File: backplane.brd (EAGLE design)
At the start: 203.2 x 101.6 mm, 14 parts, among them IC1 MAX3233ECWP

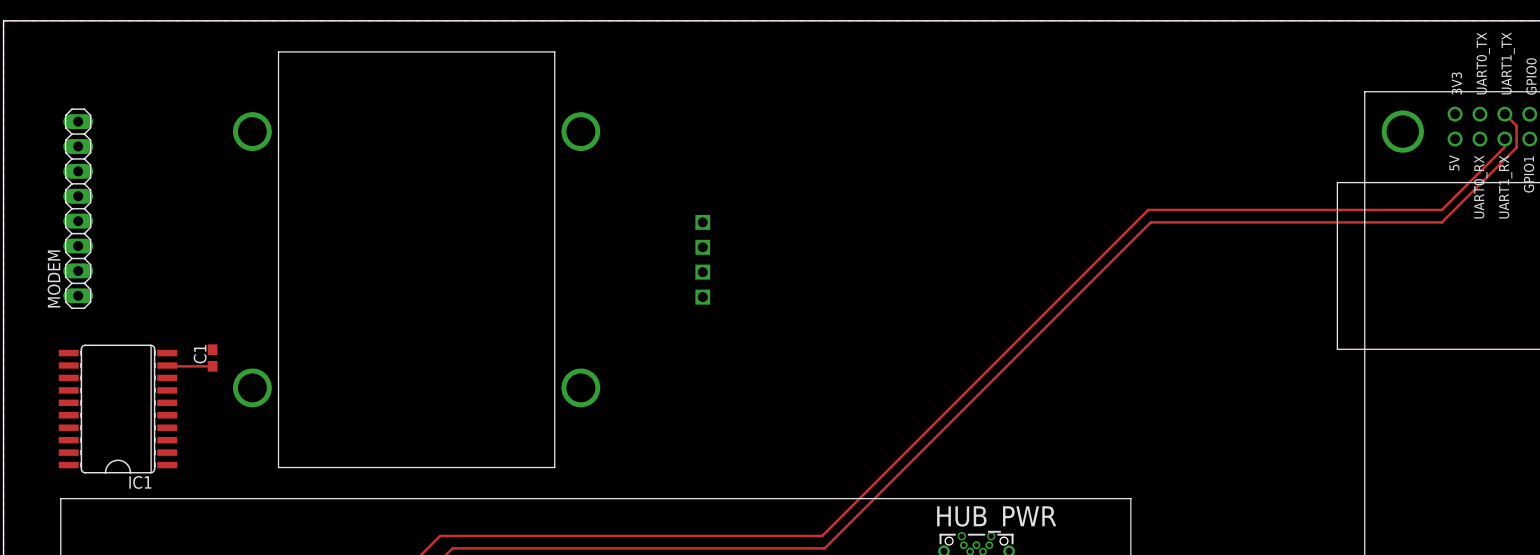
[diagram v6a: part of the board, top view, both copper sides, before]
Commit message: Add jetson - converter uart connection
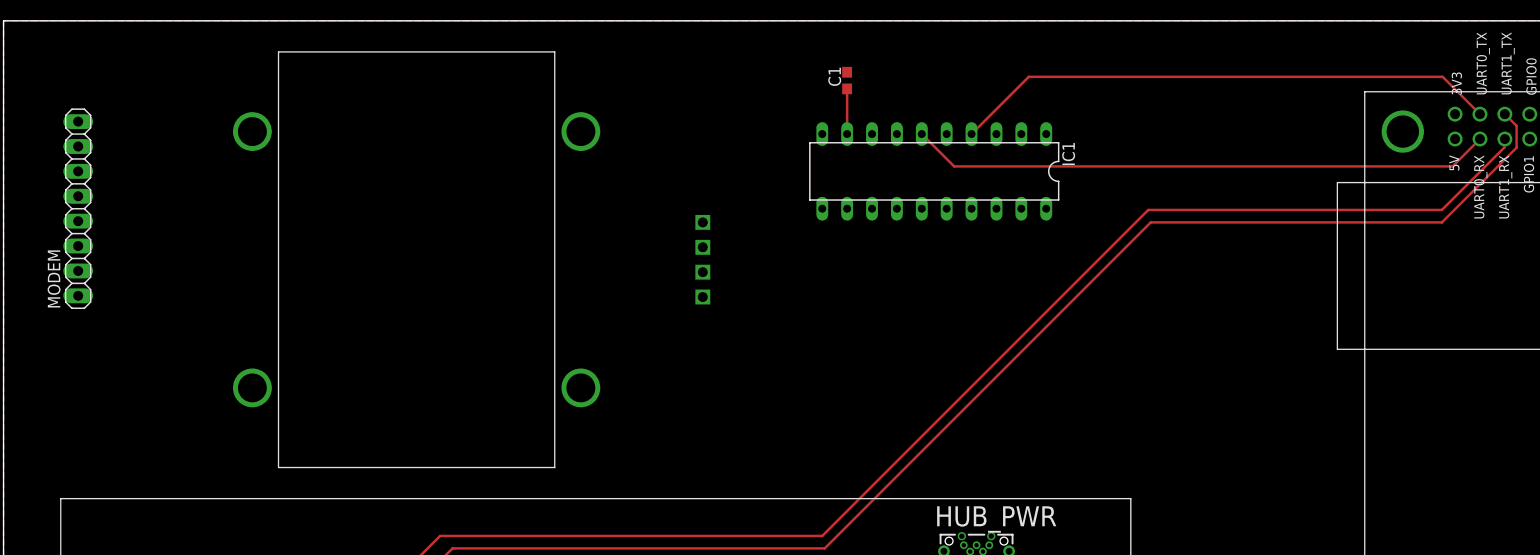
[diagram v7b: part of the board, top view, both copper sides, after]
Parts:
- C1: value (none) -> 0.1uF
- IC1: value MAX3233ECWP -> MAX3233ECPP; device auv:SO20L -> auv:DIL20
- moved IC1 86.8 mm to (95.0, 86.2), turned to 180 degrees
- moved C1 70.7 mm to (86.1, 95.5)
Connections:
- removed net SPARTON_RX: U$3.UART0_TX
- removed net SPARTON_TX: U$3.UART0_RX
- net MODEM_RS232_RX: now also IC1.7; no longer IC1.8
- net MODEM_RS232_TX: now also IC1.8; no longer IC1.7
- net MODEM_RX: now also IC1.4, U$3.UART0_TX; no longer IC1.6
- net MODEM_TX: now also IC1.6, U$3.UART0_RX; no longer IC1.4
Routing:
- net MODEM_TX: track 0.00 -> 59.5 mm
- net MODEM_RX: track 0.00 -> 55.9 mm
- added copper zone on layer 1, net GND
- added copper zone on layer 16, net VBAT
- removed copper zone on layer 16, net GND
- removed copper zone on layer 1, net VBAT
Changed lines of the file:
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@@
 <element name="PIXHAWK" library="auv" package="TE-2-5530843-0" value="PIXHAWK_EDGE_CONNCONN" x="70.612" y="30.734"/>
 <element name="MODEM" library="auv" package="1X08" value="" x="7.62" y="82.423" rot="R90"/>
-<element name="IC1" library="auv" package="SO20L" value="MAX3233ECWP" x="11.684" y="61.976" rot="R90">
-<attribute name="MF" value="MAXIM" x="11.684" y="61.976" size="1.778" layer="27" rot="R90" display="off"/>
-<attribute name="MPN" value="MAX3233ECWP" x="11.684" y="61.976" size="1.778" layer="27" rot="R90" display="off"/>
-<attribute name="OC_FARNELL" value="unknown" x="11.684" y="61.976" size="1.778" layer="27" rot="R90" display="off"/>
-<attribute name="OC_NEWARK" value="77C9167" x="11.684" y="61.976" size="1.778" layer="27" rot="R90" display="off"/>
+<element name="IC1" library="auv" package="DIL20" value="MAX3233ECPP" x="94.996" y="86.233" rot="R180">
+<attribute name="MF" value="" x="94.996" y="86.233" size="1.778" layer="27" rot="R180" display="off"/>
+<attribute name="MPN" value="MAX3233ECPP+G36" x="94.996" y="86.233" size="1.778" layer="27" rot="R180" display="off"/>
+<attribute name="OC_FARNELL" value="unknown" x="94.996" y="86.233" size="1.778" layer="27" rot="R180" display="off"/>
+<attribute name="OC_NEWARK" value="89K3596" x="94.996" y="86.233" size="1.778" layer="27" rot="R180" display="off"/>
 </element>
-<element name="C1" library="auv" package="C0603" value="" x="21.336" y="67.183" rot="R90"/>
+<element name="C1" library="auv" package="C0603" value="0.1uF" x="86.106" y="95.504" rot="R90"/>
 </elements>
 <signals>
@@
 <contactref element="HUB_PWR" pad="10"/>
 <contactref element="HUB_PWR" pad="6"/>
-<polygon width="0.1524" layer="16">
-<vertex x="203.2" y="101.6"/>
-<vertex x="0" y="101.6"/>
-<vertex x="0" y="0"/>
-<vertex x="203.2" y="0"/>
-</polygon>
 <contactref element="U$1" pad="GND"/>
 <contactref element="BAT" pad="P$2"/>
@@
 <contactref element="IC1" pad="18"/>
 <contactref element="C1" pad="2"/>
-<wire x1="6.6548" y1="58.801" x2="21.336" y2="68.033" width="0" layer="19" extent="1-1"/>
-<wire x1="8.128" y1="33.431" x2="6.6548" y2="58.801" width="0" layer="19" extent="1-1"/>
-</signal>
-<signal name="VBAT">
-<contactref element="U$3" pad="VIN"/>
 <polygon width="0.1524" layer="1">
 <vertex x="0" y="101.6"/>
@@
 <vertex x="0" y="0"/>
 </polygon>
+</signal>
+<signal name="VBAT">
+<contactref element="U$3" pad="VIN"/>
 <contactref element="BAT" pad="P$1"/>
+<polygon width="0.1524" layer="16">
+<vertex x="203.2" y="101.6"/>
+<vertex x="0" y="101.6"/>
+<vertex x="0" y="0"/>
+<vertex x="203.2" y="0"/>
+</polygon>
 </signal>
 <signal name="PIXHAWK_TELEM2_TX">
@@
 <wire x1="169.8244" y1="98.5012" x2="193.3194" y2="98.5012" width="0.254" layer="1"/>
 <wire x1="193.3194" y1="98.5012" x2="193.3194" y2="91.9988" width="0.254" layer="1"/>
-</signal>
-<signal name="SPARTON_RX">
-<contactref element="U$3" pad="UART0_TX"/>
 </signal>
 <signal name="+5V">
@@
 <wire x1="197.8406" y1="81.8388" x2="197.8406" y2="88.3412" width="0" layer="19" extent="1-1"/>
 </signal>
-<signal name="SPARTON_TX">
-<contactref element="U$3" pad="UART0_RX"/>
-</signal>
 <signal name="AHRS8_RX">
 <contactref element="U$1" pad="RX"/>
@@
 <wire x1="158.3182" y1="77.9018" x2="158.3182" y2="89.535" width="0.254" layer="16"/>
 </signal>
-<signal name="MODEM_RS232_TX">
+<signal name="MODEM_RS232_RX">
 <contactref element="IC1" pad="7"/>
 </signal>
-<signal name="MODEM_RS232_RX">
-<contactref element="IC1" pad="8"/>
-</signal>
-<signal name="MODEM_TX">
+<signal name="MODEM_RX">
+<contactref element="U$3" pad="UART0_TX"/>
 <contactref element="IC1" pad="4"/>
-</signal>
-<signal name="MODEM_RX">
-<contactref element="IC1" pad="6"/>
+<wire x1="150.6982" y1="92.075" x2="146.8882" y2="95.885" width="0.254" layer="1"/>
+<wire x1="104.648" y1="95.885" x2="98.806" y2="90.043" width="0.254" layer="1"/>
+<wire x1="146.8882" y1="95.885" x2="104.648" y2="95.885" width="0.254" layer="1"/>
 </signal>
 <signal name="+3V3">
 <contactref element="IC1" pad="9"/>
 <contactref element="C1" pad="1"/>
-<wire x1="21.336" y1="66.333" x2="16.8012" y2="66.333" width="0.254" layer="1"/>
-<wire x1="16.8012" y1="66.333" x2="16.7132" y2="66.421" width="0.254" layer="1"/>
+<wire x1="86.106" y1="94.654" x2="86.106" y2="90.043" width="0.254" layer="1"/>
+</signal>
+<signal name="MODEM_RS232_TX">
+<contactref element="IC1" pad="8"/>
+</signal>
+<signal name="MODEM_TX">
+<contactref element="IC1" pad="6"/>
+<contactref element="U$3" pad="UART0_RX"/>
+<wire x1="150.6982" y1="89.535" x2="147.9042" y2="86.741" width="0.254" layer="1"/>
+<wire x1="97.028" y1="86.741" x2="93.726" y2="90.043" width="0.254" layer="1"/>
+<wire x1="147.9042" y1="86.741" x2="97.028" y2="86.741" width="0.254" layer="1"/>
 </signal>
 </signals>
